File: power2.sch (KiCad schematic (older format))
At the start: 38 parts, among them U3 LMS6002DR2, U4 ECP5

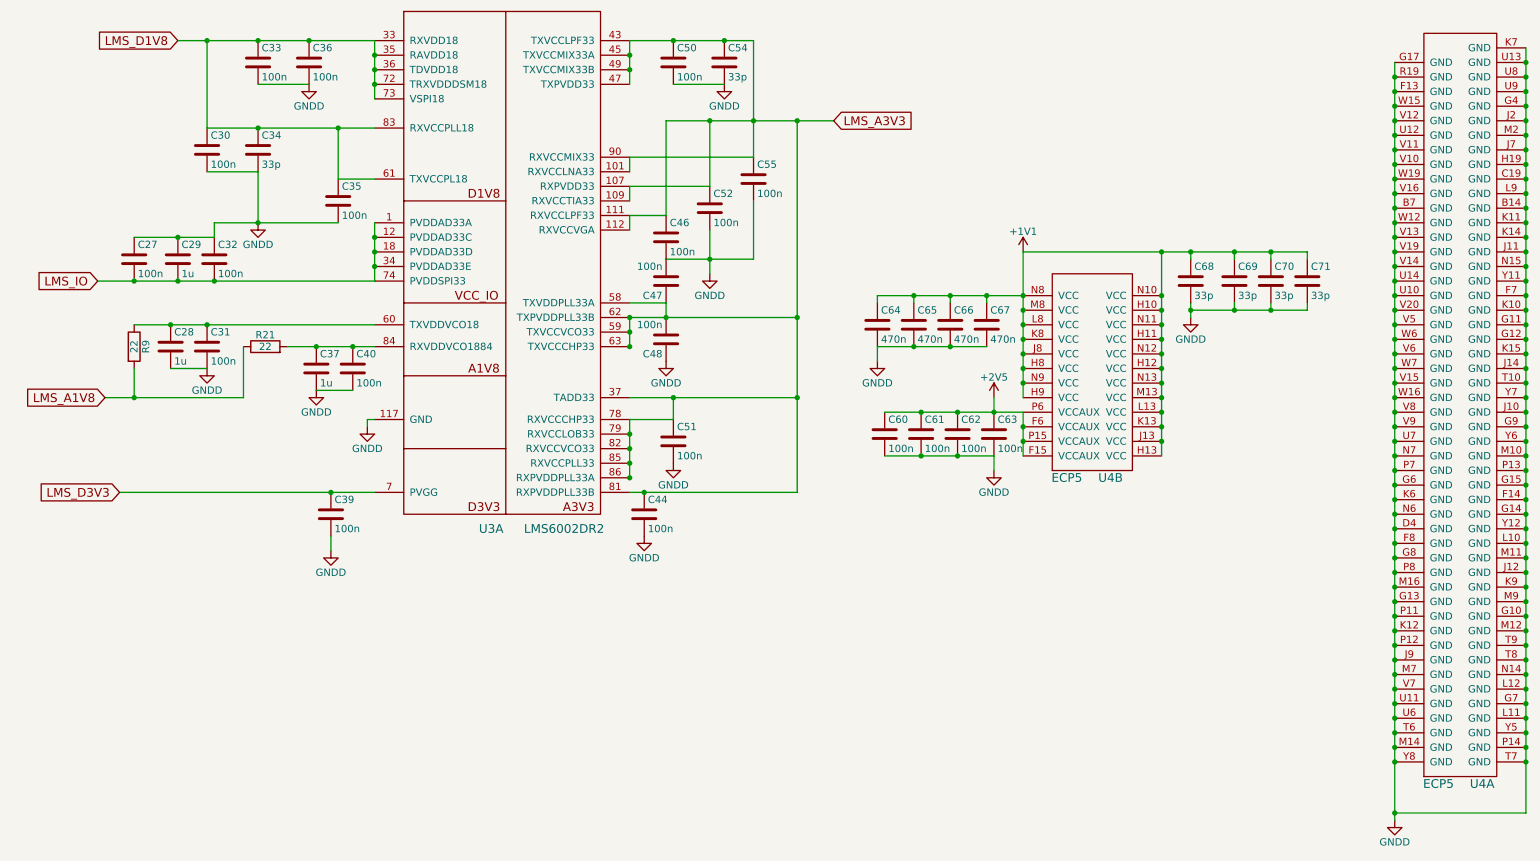
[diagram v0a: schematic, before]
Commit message: Placement of all passive is finished. Tracing of most passive is finished. RF is not started yet.
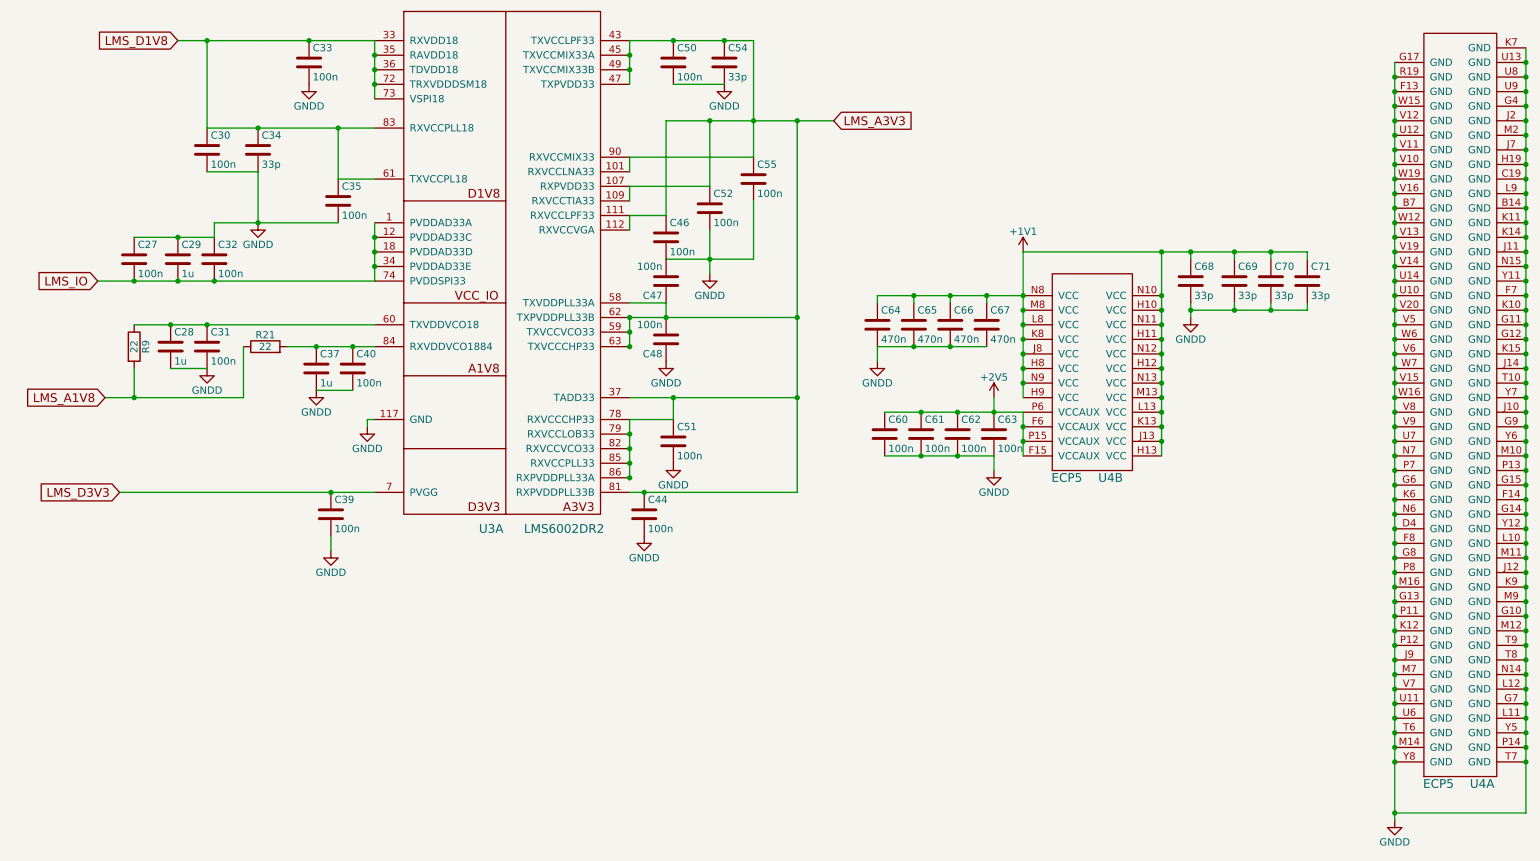
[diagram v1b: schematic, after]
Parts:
- removed C33: 100n, Capacitors_SMD:C_0603, symbol C
- renumbered C36 to C33

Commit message: Fix LMS_3V3A enable pull. Corrected shield ground
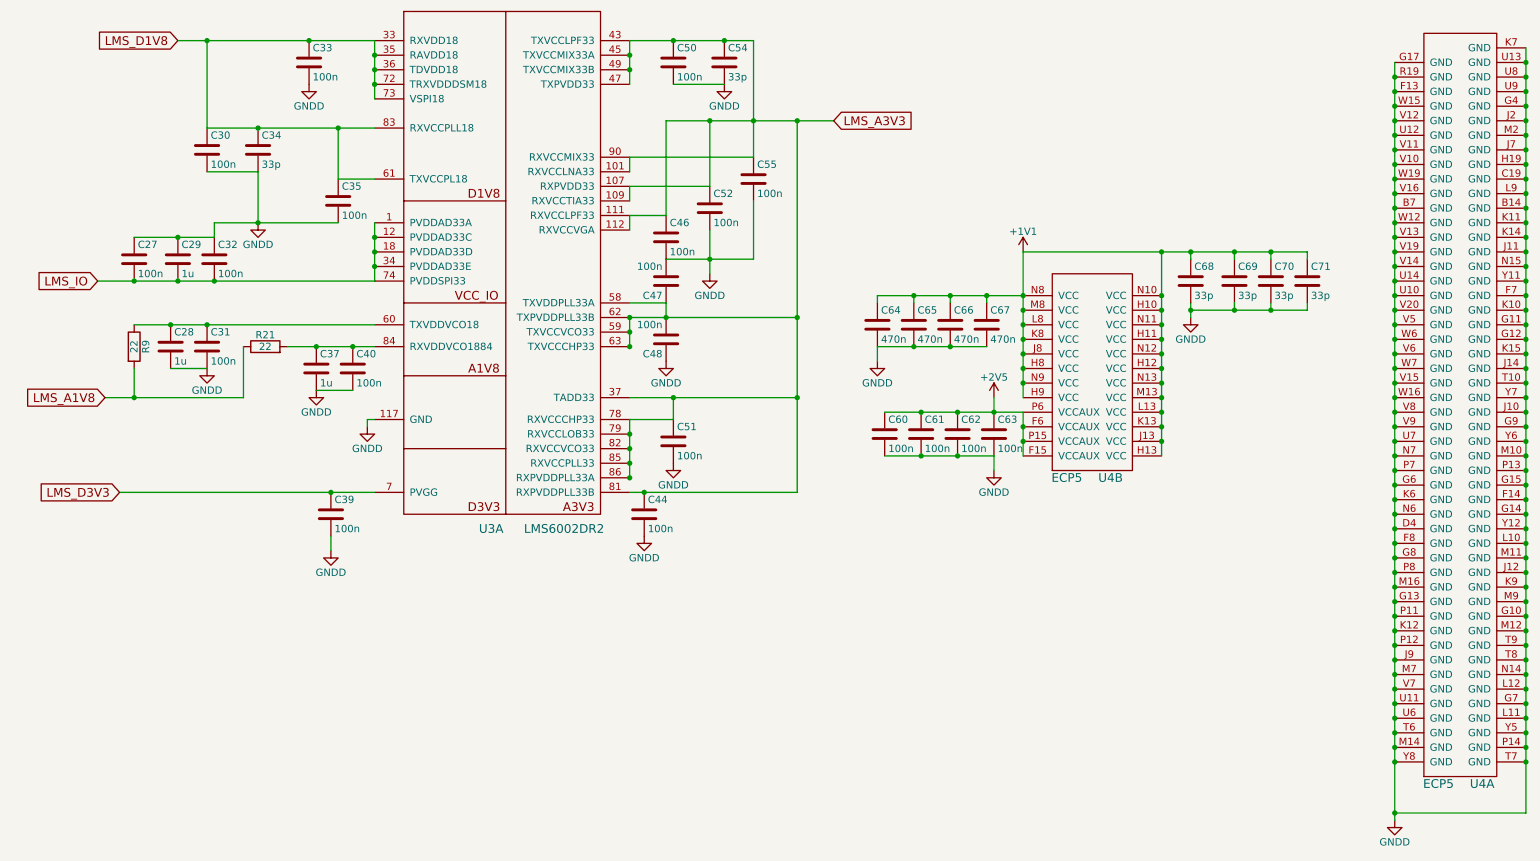
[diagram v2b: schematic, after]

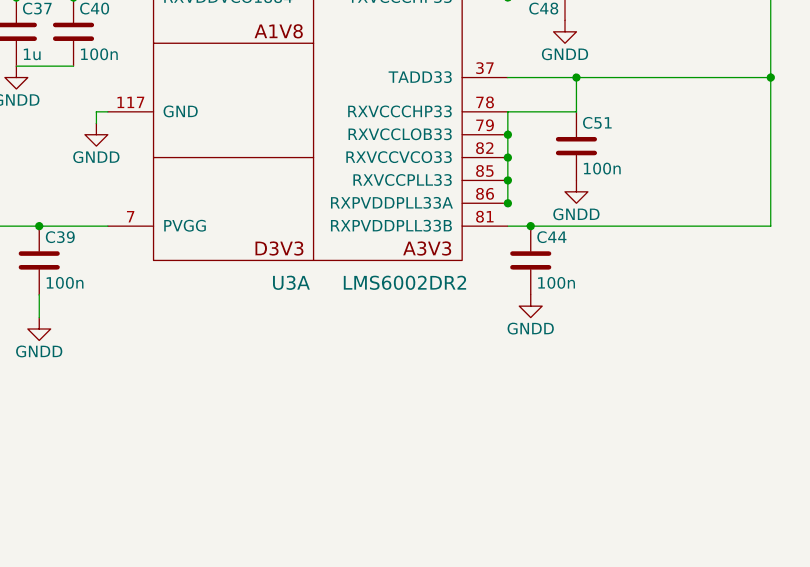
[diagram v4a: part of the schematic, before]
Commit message: Prepared BOM and changed some part numbers for unpopular ones. Added manufacture PN for each part.
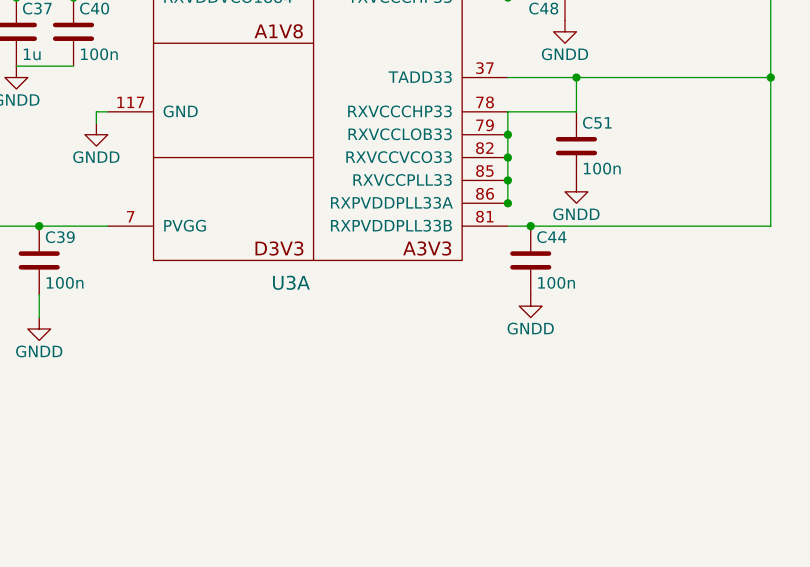
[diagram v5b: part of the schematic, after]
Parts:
- C28: manf# (none) -> GRM188R61C105KA93D
- C34: manf# (none) -> 0603YC330JAT2A
- R9: manf# (none) -> RC0603JR-0722RL
- U3: Component Value LMS6002DR2 -> (none); Vendor Digi-Key -> (none); Vendor Part Number 1434-1000-1-ND -> (none); manf# (none) -> LMS6002DFN
- U4: manf# (none) -> LFE5U-25F-6BG381I
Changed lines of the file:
@@
 LIBS:valves
 LIBS:sdr
-LIBS:usb-type-c
 LIBS:sdr-cache
 EELAYER 25 0
@@
 F 2 "sdr-foots:ECP5_381" H 8700 6450 60  0001 C CNN
 F 3 "" H 8700 6450 60  0001 C CNN
+F 4 "LFE5U-25F-6BG381I" H 10250 5900 60  0001 C CNN "manf#"
 	1    10250 5900
 	1    0    0    -1
@@
 F 2 "sdr-foots:ECP5_381" H 6150 4350 60  0001 C CNN
 F 3 "" H 6150 4350 60  0001 C CNN
+F 4 "LFE5U-25F-6BG381I" H 7700 3800 60  0001 C CNN "manf#"
 	2    7700 3800
 	1    0    0    -1
@@
 F 2 "sdr-foots:DQFN-120_via_off_pad" H 3910 6350 60  0001 C CNN
 F 3 "" H 3950 4100 60  0000 C CNN
-F 4 "1434-1000-1-ND" H 3890 6860 60  0001 C CNN "Vendor Part Number"
-F 5 "Digi-Key" H 3880 6770 60  0001 C CNN "Vendor"
-F 6 "IC, MULTI-FUNCTION, TRANSCEIVER," H 3880 6440 60  0001 C CNN "Description"
-F 7 "Lime Microsystems Ltd" H 3890 6670 60  0001 C CNN "Manufacturer"
-F 8 "LMS6002DFN" H 3880 6550 60  0001 C CNN "Manufacturer Part Number"
-F 9 "LMS6002DR2" H 4350 4000 60  0000 C CNN "Component Value"
+F 4 "LMS6002DFN" H 3950 4100 60  0001 C CNN "manf#"
+F 5 "IC, MULTI-FUNCTION, TRANSCEIVER," H 3880 6440 60  0001 C CNN "Description"
+F 6 "Lime Microsystems Ltd" H 3890 6670 60  0001 C CNN "Manufacturer"
+F 7 "LMS6002DFN" H 3880 6550 60  0001 C CNN "Manufacturer Part Number"
 	1    3950 4100
 	1    0    0    -1
@@
 F 2 "Capacitors_SMD:C_0603" H 2288 1450 50  0001 C CNN
 F 3 "" H 2250 1600 50  0000 C CNN
+F 4 "0603YC330JAT2A" H 2250 1600 60  0001 C CNN "manf#"
 	1    2250 1600
 	1    0    0    -1
@@
 F 2 "Resistors_SMD:R_0603" V 1330 2950 50  0001 C CNN
 F 3 "" H 1400 2950 50  0000 C CNN
+F 4 "RC0603JR-0722RL" H 1400 2950 60  0001 C CNN "manf#"
 	1    1400 2950
 	1    0    0    -1
@@
 F 2 "Capacitors_SMD:C_0603" H 1688 2800 50  0001 C CNN
 F 3 "" H 1650 2950 50  0000 C CNN
+F 4 "GRM188R61C105KA93D" H 1650 2950 60  0001 C CNN "manf#"
 	1    1650 2950
 	1    0    0    -1
